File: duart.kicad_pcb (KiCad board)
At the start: 2 copper layers, 99.1 x 49.9 mm, 39 parts, among them P1 RC2014_STANDARD_DEV_39, P2 SERIALA, P3 SERIALB, P4 OUTPUT, P5 INPUT, P6 POWER, P7 IEO/IEI, SW1 Switch_DIP_4, U1 74HCT74, U2 74HCT688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

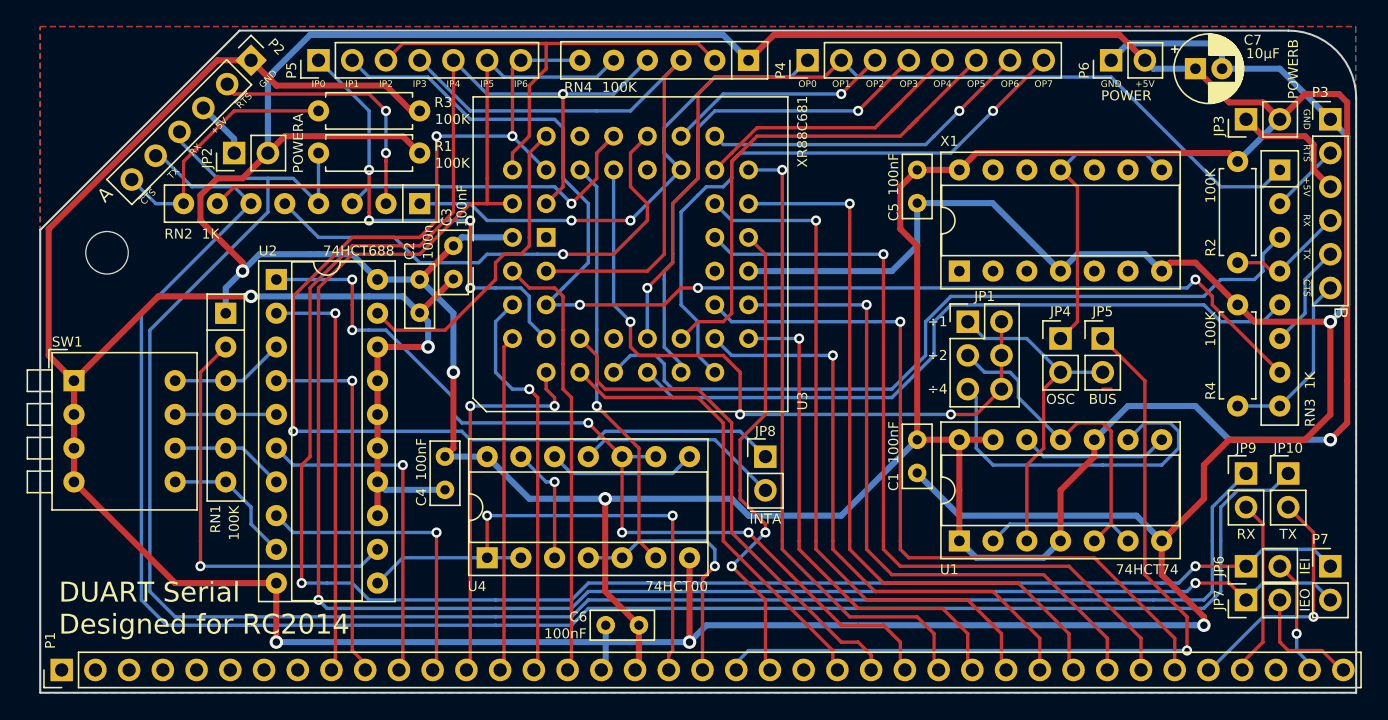
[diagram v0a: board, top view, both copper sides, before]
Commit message: move JP4/JP5 and JP9/JP10 pairs closer together so 2x2 pin headers can be used
adjust some text
 make references for C2 and C3 easier to read
 don't use tab characters in text, OSH Park renders it as a question mark

add link to repository
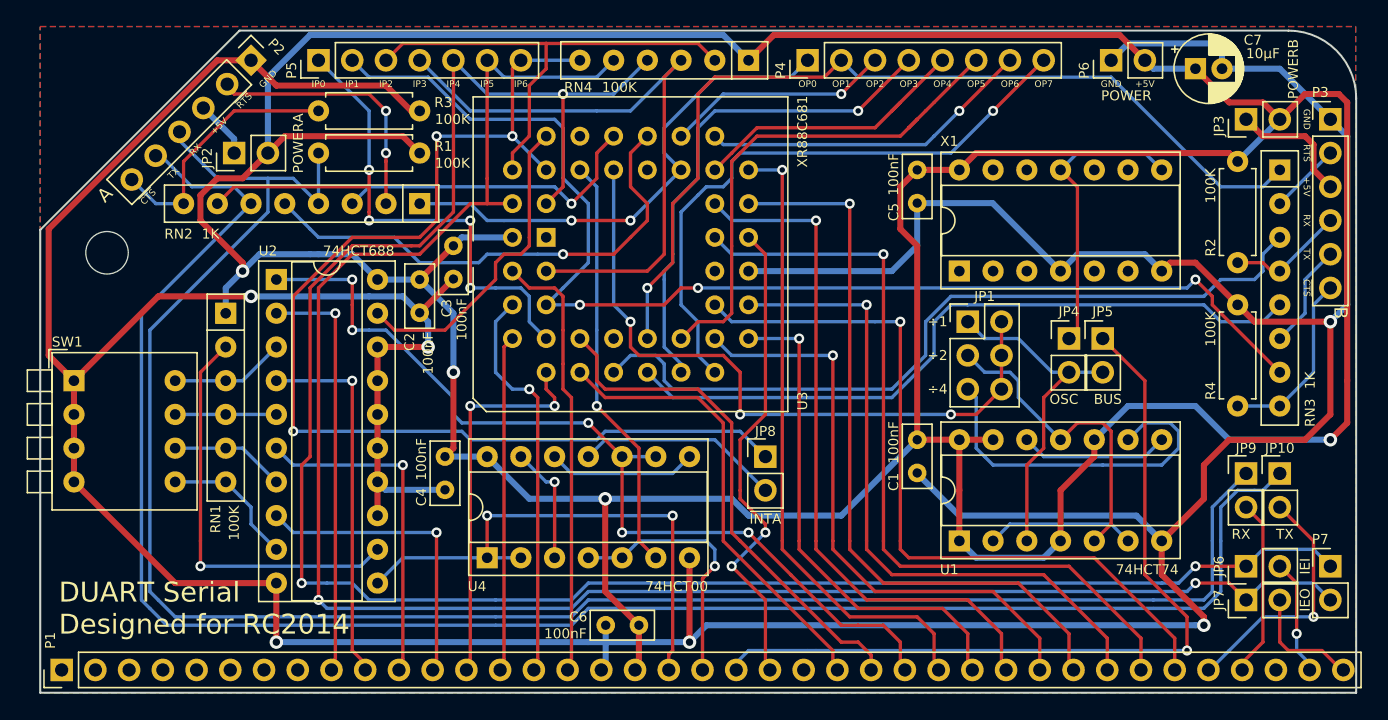
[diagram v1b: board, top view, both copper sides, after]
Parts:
- moved JP10 0.63 mm to (182.2, 121.9)
- moved JP4 0.63 mm to (166.4, 111.8)
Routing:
- net /TXA: track 137.5 -> 136.9 mm
- net (no net): track 0.63 -> 0.00 mm
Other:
- board text added: "20200407 ©2019-2020 Chris Odorjan https://github.com/codorjan/duart"
- board text added: "SW1 = upper nibble of base address (on/dn = binary 0, off/up = binary 1)"
- board text removed: "100n"
- board text removed: "20200219 Copyright ©2019-2020 Chris Odorjan"
- board text removed: "SW1 = upper nibble of base address (on = binary 0, off = binary 1)"
